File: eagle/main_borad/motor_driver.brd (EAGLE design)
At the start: 52 x 42 mm, 19 parts, among them IC1 MEGA8-AI, Y1 16MHz

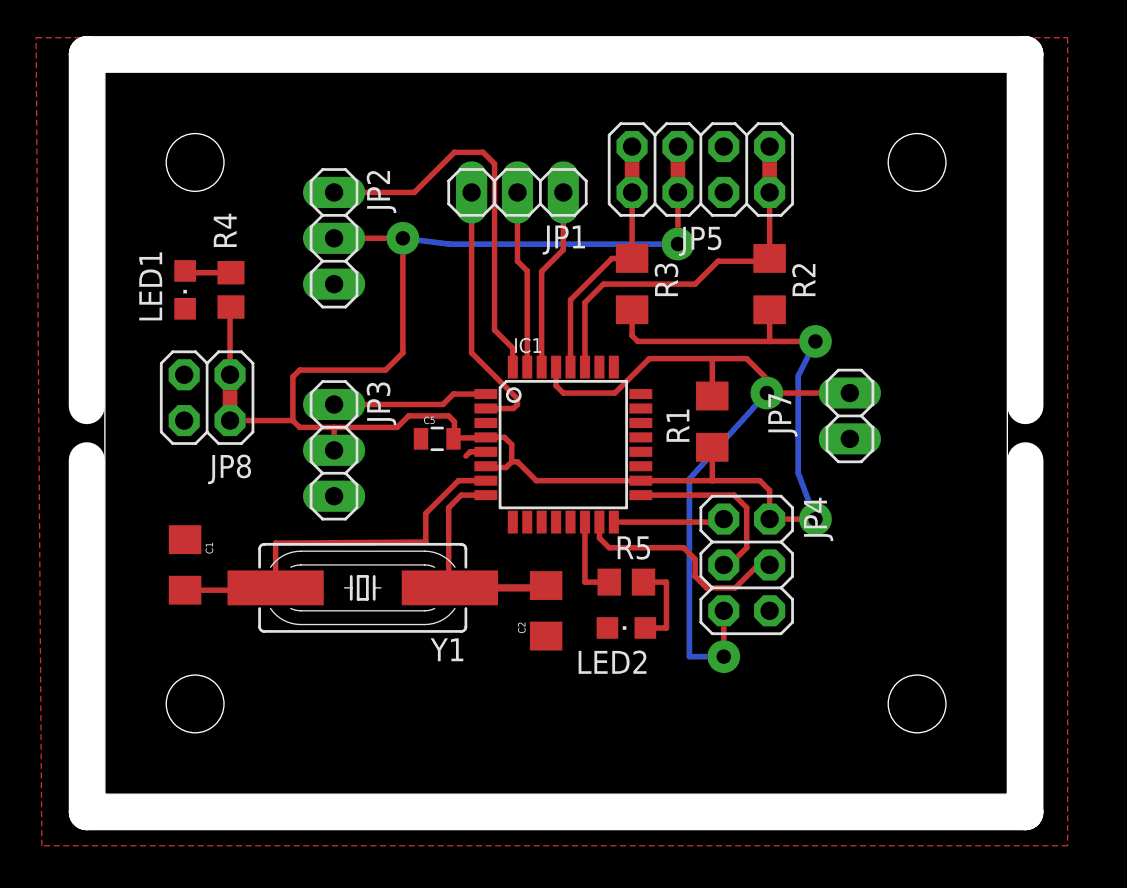
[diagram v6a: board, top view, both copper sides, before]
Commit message: Repaired motor_driver PCB
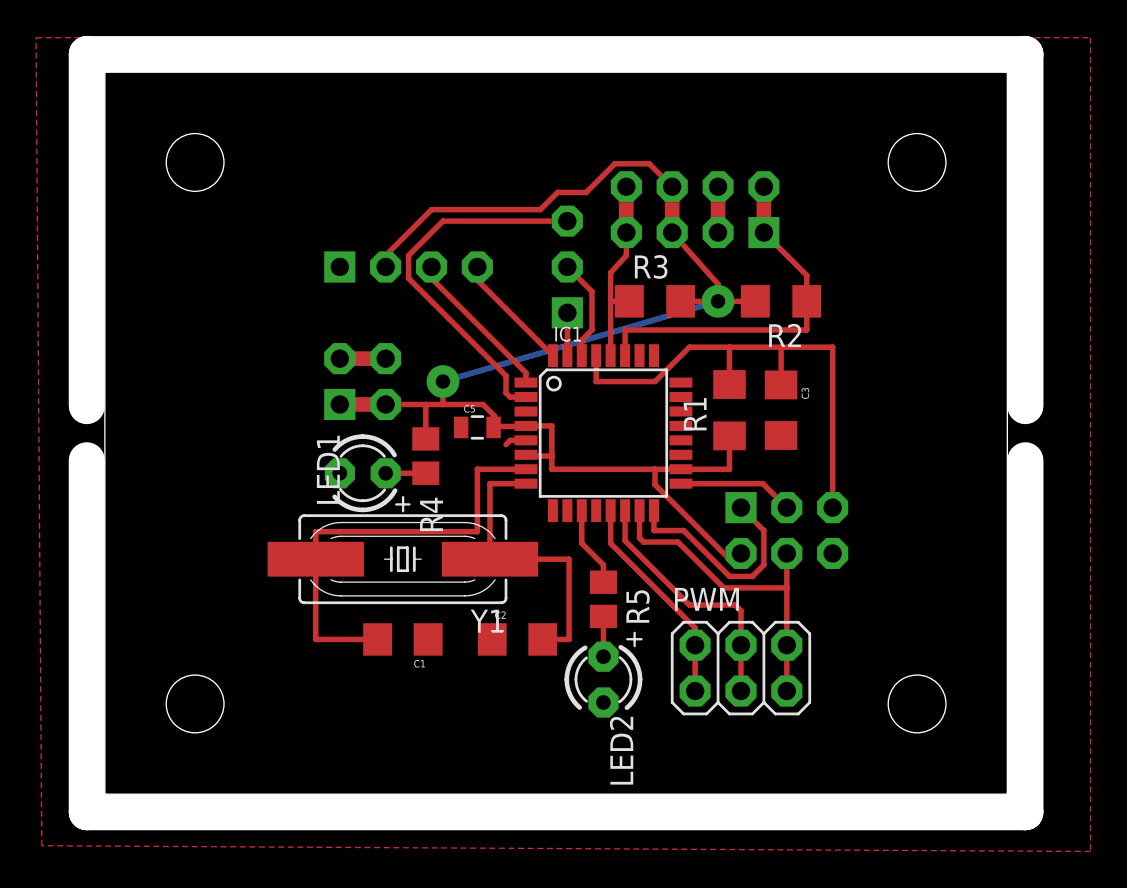
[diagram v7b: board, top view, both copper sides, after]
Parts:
- removed JP3: (no value), pinhead:1X03
- removed JP7: (no value), pinhead:1X02
- added C3: 4n7, SparkFun-Capacitors:1206
- added PWM: (no value), pinhead:2X03
- JP1: value (none) -> serial; device pinhead:1X03 -> pinhead-2:1X03-S
- JP2: value (none) -> encoder; device pinhead:1X03 -> pinhead-2:1X04-S
- JP4: value (none) -> ICSP; device pinhead:2X03 -> pinhead-2:2X03
- JP5: value (none) -> i2c; device pinhead:2X04 -> pinhead-2:2X04
- JP8: value (none) -> power; device pinhead:2X02 -> pinhead-2:2X02
- LED1: value (none) -> OF-SMD-2012G-1; device adafruit:CHIPLED_0805 -> adafruit:LED3MM
- LED2: value (none) -> OF-SMD2012R; device adafruit:CHIPLED_0805 -> adafruit:LED3MM
- R2, R3: value 5k -> 4k7
- moved R4 14.2 mm to (17.8, 18.7), turned to 270 degrees
- moved LED1 14.1 mm to (14.3, 17.8)
- moved C1 12.8 mm to (16.5, 8.57), turned to 180 degrees
- moved JP8 8.67 mm to (14.3, 22.9), flipped to the bottom, turned to 90 degrees
- moved JP1 4.97 mm to (25.6, 29.2), flipped to the bottom, turned to 90 degrees
- moved JP2 4.42 mm to (16.8, 29.2), flipped to the bottom, turned to 180 degrees
- moved LED2 3.13 mm to (27.6, 6.35), turned to 270 degrees
- moved JP4 2.93 mm to (37.8, 14.6), flipped to the bottom, turned to 180 degrees
- moved Y1 2.73 mm to (16.5, 13.0)
- moved C5 2.31 mm to (20.6, 20.3)
- moved IC1 2.31 mm to (27.6, 20.0)
- moved JP5 2.25 mm to (32.7, 32.4), flipped to the bottom, turned to 0 degrees
- moved C2 2.25 mm to (22.9, 8.57), turned to 0 degrees
- moved R3 1.59 mm to (30.5, 27.3), turned to 0 degrees
- moved R5 1.59 mm to (27.6, 10.8), turned to 270 degrees
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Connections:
- removed net N$7: IC1.15, JP4.4
- new net MOSI/PWM2: IC1.15, JP4.4, PWM.5, PWM.6
- new net PWM1A: IC1.13, PWM.1, PWM.2
- new net PWM1B: IC1.14, PWM.3, PWM.4
- net GND: now also C3.2, JP2.1, LED1.K, LED2.K; no longer JP2.3, JP3.3, JP7.2, LED1.C, LED2.C
- net INT0: now also JP2.4; no longer JP2.1
- net INT1: now also JP2.3; no longer JP3.1
- net N$1: now also JP1.1; no longer JP1.2
- net N$4: now also IC1.11; no longer IC1.14
- net N$5: now also JP1.2; no longer JP1.1
- net RESET: now also C3.1; no longer JP7.1
- net VCC: no longer JP3.2
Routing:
- net VCC: track 112.5 -> 85.3 mm, vias 4 -> 2
- net MOSI/PWM2: track 0.00 -> 18.4 mm
- net INT0: track 21.8 -> 6.65 mm
- net PWM1B: track 0.00 -> 14.1 mm
- net RESET: track 42.3 -> 28.4 mm, vias 2 -> 0
- net N$7: track 12.5 -> 0.00 mm
- net PWM1A: track 0.00 -> 11.9 mm
- net N$1: track 9.90 -> 2.37 mm
- net N$6: track 14.6 -> 20.6 mm
- net N$13: track 6.26 -> 12.2 mm
- net GND: track 1.20 -> 6.28 mm
- net N$5: track 10.2 -> 5.71 mm
- net N$2: track 12.3 -> 16.5 mm
- net N$12: track 10.0 -> 6.42 mm
- net N$9: track 14.3 -> 10.7 mm
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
